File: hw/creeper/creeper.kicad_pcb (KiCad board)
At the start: 2 copper layers, 35 x 35 mm, 19 parts, among them SW1 EG1218, U1 ATtiny85V-10SU, U2 LIS2DH12TR

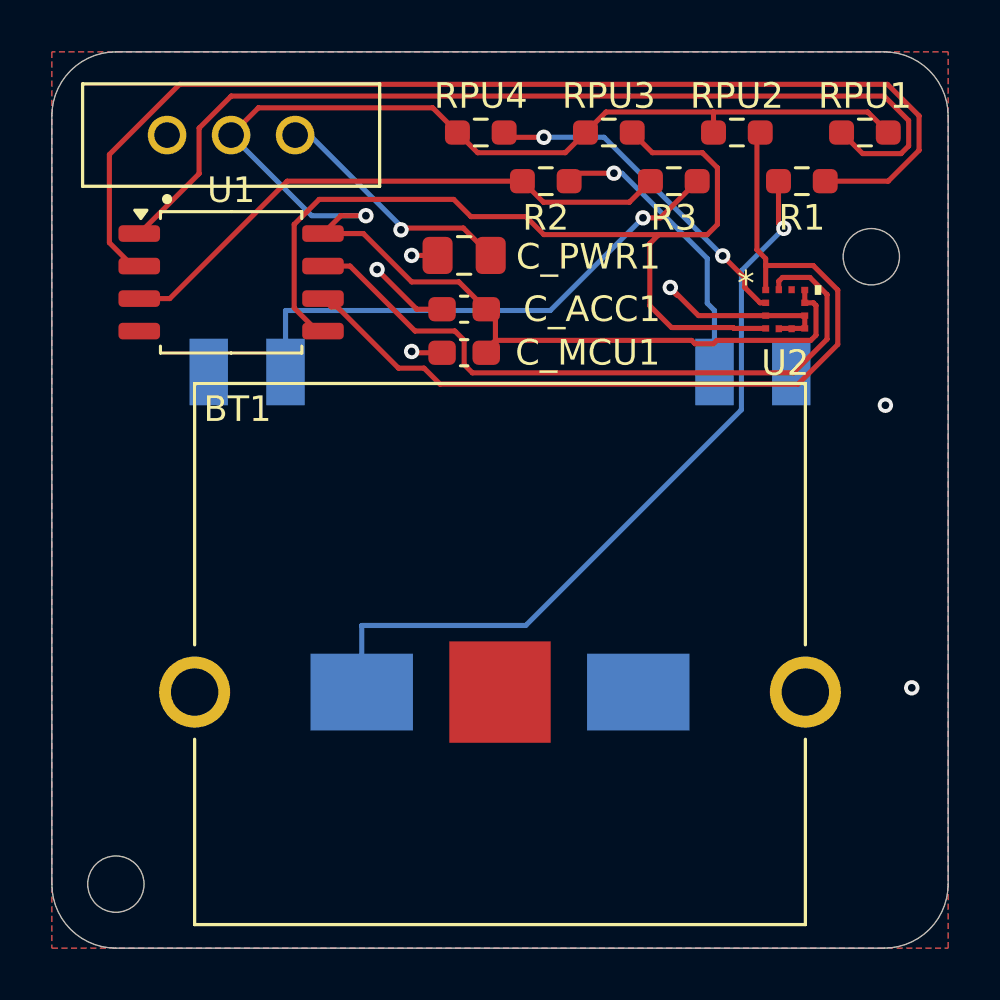
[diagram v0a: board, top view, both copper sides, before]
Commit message: feat(pcb): v0.7
* added TC2030_AVR pogo debug plug connector
* added isolating resistors to stabilize ISP
* fixed missing connections of battery holder
* added 0R bridge for always-on w/o switch
* moved mounting hole out of case opening
* did manual place and route
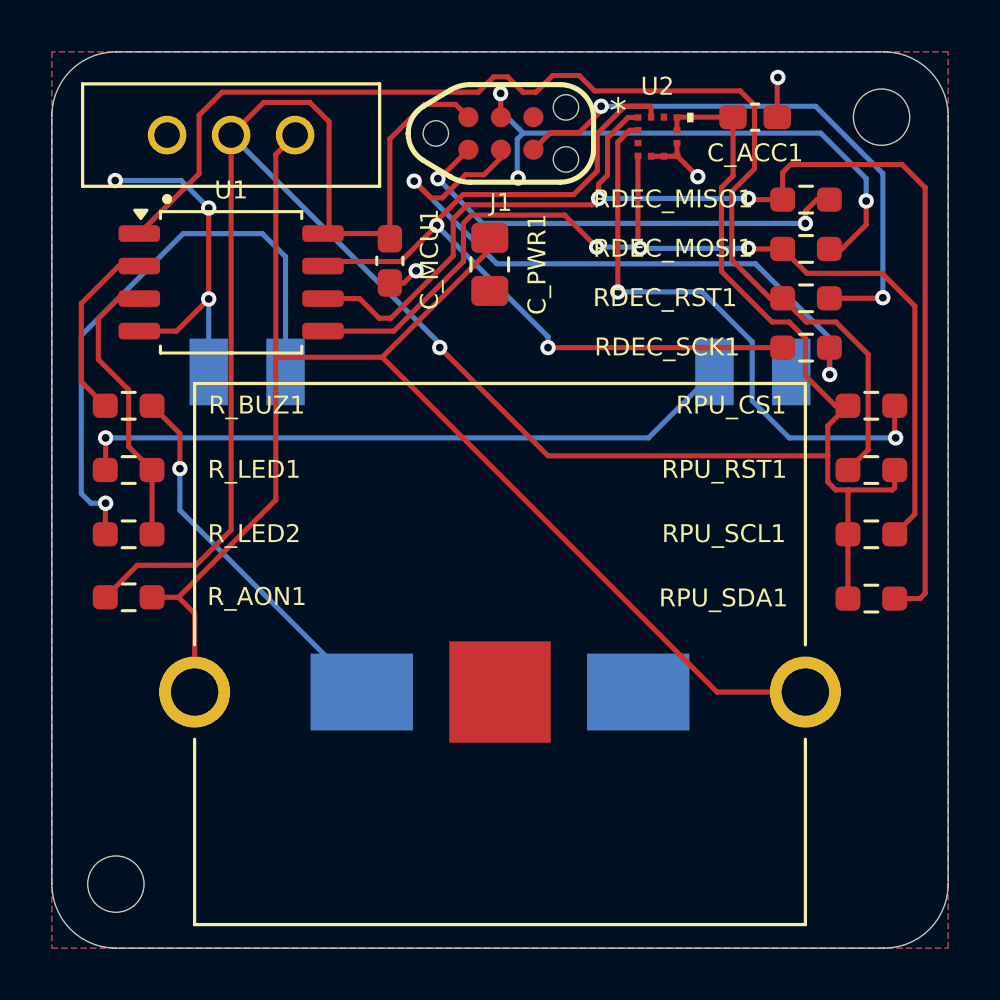
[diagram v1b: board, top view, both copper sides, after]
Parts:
- removed R1: 0R, Resistor_SMD:R_0603_1608Metric_Pad0.98x0.95mm_HandSolder
- removed R2, R3: 43R, Resistor_SMD:R_0603_1608Metric_Pad0.98x0.95mm_HandSolder
- removed RPU1, RPU2, RPU3, RPU4: 10K, Resistor_SMD:R_0603_1608Metric_Pad0.98x0.95mm_HandSolder
- added J1: TC2030_AVR, PCM_marbastlib-various:CON_TC2030_outlined, F.Cu at (117.5, 53.2)
- added RDEC_MISO1: 100R, Resistor_SMD:R_0603_1608Metric_Pad0.98x0.95mm_HandSolder, F.Cu at (129.4, 55.8)
- added RDEC_MOSI1: 100R, Resistor_SMD:R_0603_1608Metric_Pad0.98x0.95mm_HandSolder, F.Cu at (129.4, 57.7)
- added RDEC_RST1: 100R, Resistor_SMD:R_0603_1608Metric_Pad0.98x0.95mm_HandSolder, F.Cu at (129.4, 59.6)
- added RDEC_SCK1: 100R, Resistor_SMD:R_0603_1608Metric_Pad0.98x0.95mm_HandSolder, F.Cu at (129.4, 61.5)
- added RPU_CS1: 10K, Resistor_SMD:R_0603_1608Metric_Pad0.98x0.95mm_HandSolder, F.Cu at (132.0, 63.8)
- added RPU_RST1: 10K, Resistor_SMD:R_0603_1608Metric_Pad0.98x0.95mm_HandSolder, F.Cu at (132.0, 66.3)
- added RPU_SCL1: 10K, Resistor_SMD:R_0603_1608Metric_Pad0.98x0.95mm_HandSolder, F.Cu at (132.0, 68.8)
- added RPU_SDA1: 10K, Resistor_SMD:R_0603_1608Metric_Pad0.98x0.95mm_HandSolder, F.Cu at (132.0, 71.3)
- added R_AON1: 0R, Resistor_SMD:R_0603_1608Metric_Pad0.98x0.95mm_HandSolder, F.Cu at (103.0, 71.3)
- added R_BUZ1: 0R, Resistor_SMD:R_0603_1608Metric_Pad0.98x0.95mm_HandSolder, F.Cu at (103.0, 63.8)
- added R_LED1: 43R, Resistor_SMD:R_0603_1608Metric_Pad0.98x0.95mm_HandSolder, F.Cu at (103.0, 66.3)
- added R_LED2: 43R, Resistor_SMD:R_0603_1608Metric_Pad0.98x0.95mm_HandSolder, F.Cu at (103.0, 68.8)
- moved C_ACC1 13.6 mm to (127.5, 52.5), turned to 0 degrees
- moved U2 8.38 mm to (123.7, 53.3)
- moved REF**2 5.46 mm to (132.4, 52.5)
- moved C_MCU1 4.61 mm to (113.2, 58.2), turned to -90 degrees
- moved C_PWR1 1.06 mm to (117.1, 58.3), turned to -90 degrees
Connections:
- U1 pad 1: Net-(U1-~{RESET}/PB5) -> /~RESET
- U2 pad 3: GND -> unconnected-(U2-SDO/SA0-Pad3)
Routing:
- net Net-(BT1-+): track 9.72 -> 57.4 mm, vias 1 -> 0
- net /~RESET: track 0.00 -> 47.0 mm
- net Net-(U1-~{RESET}/PB5): track 37.8 -> 0.00 mm
- net /BUZZER: track 43.8 -> 7.25 mm
- net /+3V: track 61.6 -> 97.4 mm
- net Net-(J1-SCK): track 0.00 -> 25.9 mm, vias 0 -> 2
- net Net-(J1-MOSI): track 0.00 -> 22.5 mm, vias 0 -> 3
- net Net-(J1-~{RST}): track 0.00 -> 22.5 mm, vias 0 -> 2
- net Net-(J1-MISO): track 0.00 -> 18.3 mm, vias 0 -> 2
- net Net-(BZ1-+): track 30.6 -> 14.6 mm
- net /SCL: track 33.8 -> 49.3 mm, vias 0 -> 2
- net Net-(D1-A): track 11.5 -> 26.1 mm
- net /LED: track 22.5 -> 11.2 mm
- net Net-(U2-CS): track 13.2 -> 22.7 mm
- net GND: track 12.8 -> 19.2 mm
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
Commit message: feat: rev. 0.10: use analog switch for programmer isolation
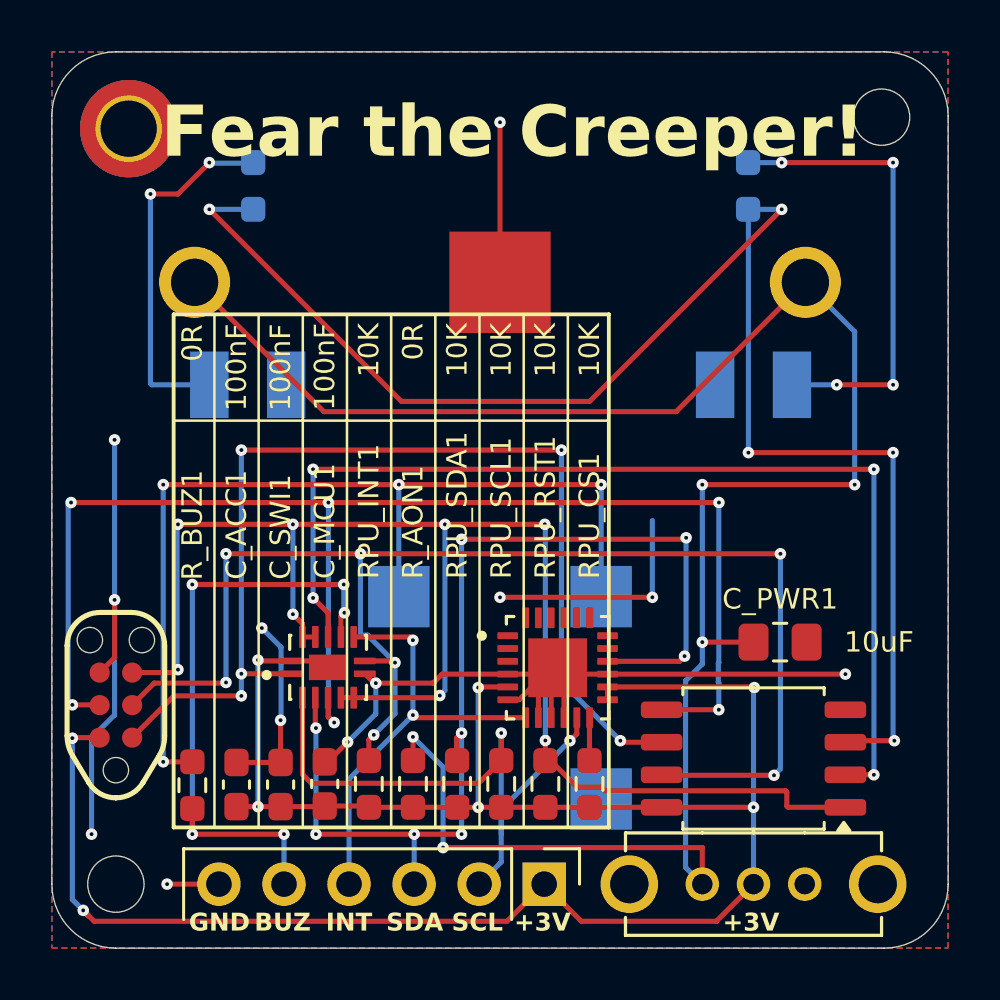
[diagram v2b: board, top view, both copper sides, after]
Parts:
- removed RDEC_MISO1, RDEC_MOSI1, RDEC_RST1, RDEC_SCK1: 100R, Resistor_SMD:R_0603_1608Metric_Pad0.98x0.95mm_HandSolder
- added C_SWI1: 100nF, creeper:C_0603_1608Metric_Pad1.08x0.95mm_HandSolder, F.Cu at (108.9, 78.6)
- added J2: Conn_01x06_Pin, creeper:PinHeader_1x06_P2.54mm_Vertical, F.Cu at (119.2, 82.5)
- added REF**: MountingHole_2.2mm_M2_DIN965_Pad_TopBottom, MountingHole:MountingHole_2.2mm_M2_DIN965_Pad_TopBottom, F.Cu at (103.0, 53.0)
- added RPU_INT1: 10K, creeper:R_0603_1608Metric_Pad0.98x0.95mm_HandSolder, F.Cu at (112.4, 78.6)
- added U3: ~, creeper:QFN50P300X250X100-15N, F.Cu at (110.8, 74.0)
- BZ1: value SMT-1324-TW-1V-HT-R -> ~; footprint creeper:XDCR_SMT-1324-TW-1V-HT-R -> creeper:XDCR_SMT-0825-S-2-R
- C_ACC1, C_MCU1: footprint Capacitor_SMD:C_0603_1608Metric_Pad1.08x0.95mm_HandSolder -> creeper:C_0603_1608Metric_Pad1.08x0.95mm_HandSolder
- C_PWR1: footprint Capacitor_SMD:C_0805_2012Metric_Pad1.18x1.45mm_HandSolder -> creeper:C_0805_2012Metric_Pad1.18x1.45mm_HandSolder
- RPU_CS1, RPU_RST1, RPU_SCL1, RPU_SDA1, R_AON1, R_BUZ1: footprint Resistor_SMD:R_0603_1608Metric_Pad0.98x0.95mm_HandSolder -> creeper:R_0603_1608Metric_Pad0.98x0.95mm_HandSolder
- R_LED1, R_LED2: value 43R -> 100R; footprint Resistor_SMD:R_0603_1608Metric_Pad0.98x0.95mm_HandSolder -> creeper:R_0603_1608Metric_Pad0.98x0.95mm_HandSolder; moved to B.Cu
- SW1: value EG1218 -> EG1213; footprint creeper:SW_EG1218 -> creeper:SW_EG1213
- U1: footprint Package_SO:SOIC-8_5.3x5.3mm_P1.27mm -> creeper:SOIC-8_5.3x5.3mm_P1.27mm
- U2: value LIS2DH12TR -> IIS328DQTR; footprint creeper:LGA-12_STM -> creeper:IIS328DQTR_QFN50P400X400X185-25N
- moved SW1 35.7 mm to (127.4, 82.5), turned to 180 degrees
- moved C_ACC1 33.0 mm to (107.2, 78.6), turned to 90 degrees
- moved U1 27.6 mm to (127.4, 77.6), turned to 180 degrees
- moved J1 26.9 mm to (102.5, 75.5), turned to 90 degrees
- moved R_LED1 26.6 mm to (127.2, 55.2), turned to -90 degrees
- moved U2 21.1 mm to (119.8, 74.0)
- moved C_MCU1 20.6 mm to (110.7, 78.6), turned to 90 degrees
- moved C_PWR1 18.6 mm to (128.4, 73.0), turned to 0 degrees
- moved RPU_CS1 18.4 mm to (121.0, 78.6), turned to -90 degrees
- moved RPU_SDA1 17.7 mm to (115.8, 78.6), turned to 90 degrees
- moved RPU_RST1 17.7 mm to (119.3, 78.6), turned to 90 degrees
- moved RPU_SCL1 17.4 mm to (117.5, 78.6), turned to 90 degrees
- moved BT1 16.0 mm to (117.5, 59.0), turned to 180 degrees
- moved R_BUZ1 15.0 mm to (105.5, 78.6), turned to 90 degrees
- moved R_LED2 14.4 mm to (107.9, 55.2), turned to -90 degrees
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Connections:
- net /LED renamed /LED_MCU
- J1 pad 1: Net-(J1-MISO) -> /SCL_MCU
- J1 pad 3: Net-(J1-SCK) -> /INT_MCU
- J1 pad 4: Net-(J1-MOSI) -> /SDA_MCU
- J1 pad 5: Net-(J1-~{RST}) -> /~RESET
- RPU_CS1 pad 1: /+3V -> Net-(U2-CS)
- RPU_CS1 pad 2: Net-(U2-CS) -> /+3V
- RPU_RST1 pad 1: /~RESET -> /+3V
- RPU_RST1 pad 2: /+3V -> /~RESET
- RPU_SCL1 pad 2: /SDA -> /SCL1
- RPU_SDA1 pad 2: /SCL -> /SDA1
- R_BUZ1 pad 1: /BUZZER -> /BUZ
- U1 pad 2: /BUZZER -> /BUZ_MCU
- U1 pad 5: /SDA -> /SDA_MCU
- U1 pad 6: /SCL -> /SCL_MCU
- U1 pad 7: /INT -> /INT_MCU
- U2 pad 1: /SCL -> (no net)
- U2 pad 10: /+3V -> GND
- U2 pad 11: unconnected-(U2-INT2-Pad11) -> /SCL1
- U2 pad 12: /INT -> Net-(U2-CS)
- U2 pad 2: Net-(U2-CS) -> (no net)
- U2 pad 4: /SDA -> GND
- U2 pad 5: GND -> /+3V
- U2 pad 7: GND -> /INT
- U2 pad 9: /+3V -> GND
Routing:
- net GND: track 19.2 -> 74.7 mm, vias 6 -> 12
- net /INT_MCU: track 0.00 -> 54.2 mm, vias 0 -> 7
- net /SDA_MCU: track 0.00 -> 54.2 mm, vias 0 -> 6
- net /SCL: track 49.3 -> 0.00 mm, vias 2 -> 0
- net /LED_MCU: track 11.2 -> 59.6 mm, vias 0 -> 5
- net /SCL_MCU: track 0.00 -> 42.8 mm, vias 0 -> 5
- net /SDA1: track 0.00 -> 42.0 mm, vias 0 -> 8
- net /BUZ_MCU: track 0.00 -> 41.7 mm, vias 0 -> 4
- net /SDA: track 40.2 -> 0.00 mm, vias 3 -> 0
- net Net-(J1-SCK): track 25.9 -> 0.00 mm, vias 2 -> 0
- net /SCL1: track 0.00 -> 24.4 mm, vias 0 -> 2
- net /BUZ: track 0.00 -> 24.2 mm, vias 0 -> 5
- net Net-(BZ1-Pad1): track 14.6 -> 37.7 mm, vias 1 -> 4
- net Net-(J1-MOSI): track 22.5 -> 0.00 mm, vias 3 -> 0
- net Net-(J1-~{RST}): track 22.5 -> 0.00 mm, vias 2 -> 0
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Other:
- board text added: "+3V"
- board text added: "BUZ"
- board text added: "GND"
- board text added: "INT"
- board text added: "SCL"
- board text added: "SDA"

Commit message: feat(pcb): update constraints, fix via sizes
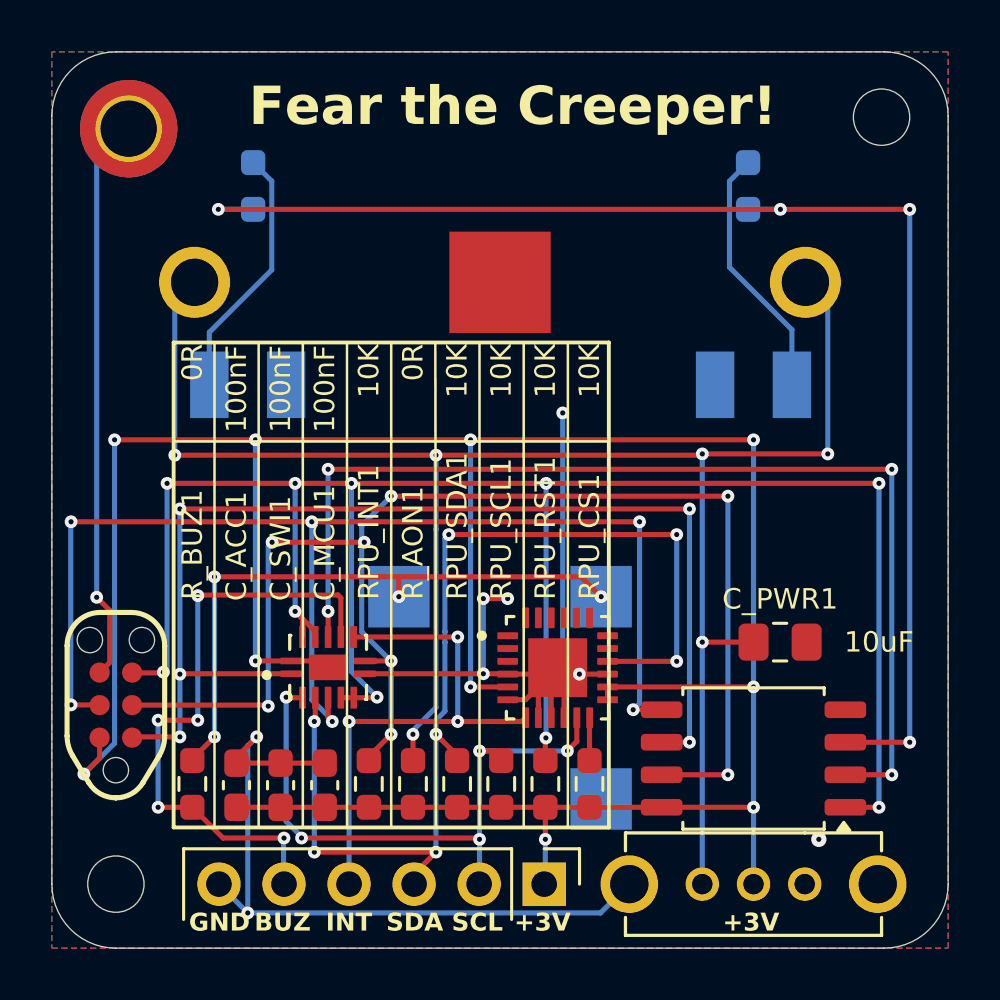
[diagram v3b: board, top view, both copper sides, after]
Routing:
- net /+3V: track 85.3 -> 109.6 mm, vias 8 -> 10
- net /~RESET: track 59.4 -> 79.0 mm, vias 8 -> 10
- net Net-(BZ1-Pad1): track 37.7 -> 23.8 mm
- net GND: track 74.7 -> 83.1 mm, vias 12 -> 9
- net Net-(D1-A): track 18.2 -> 9.99 mm, vias 4 -> 0
- net Net-(BT1-+): track 78.2 -> 70.8 mm, vias 5 -> 6
- net /LED_MCU: track 59.6 -> 53.0 mm, vias 5 -> 4
- net /SDA_MCU: track 54.2 -> 48.2 mm
- net Net-(D2-A): track 14.2 -> 9.99 mm, vias 2 -> 0
- net /INT: track 17.4 -> 20.6 mm, vias 2 -> 3
- net /SCL_MCU: track 42.8 -> 45.2 mm
- net /SDA1: track 42.0 -> 42.9 mm, vias 8 -> 7
- net /INT_MCU: track 54.2 -> 55.0 mm, vias 7 -> 8
- net /BUZ_MCU: track 41.7 -> 42.3 mm
- net /SCL1: track 24.4 -> 24.5 mm, vias 2 -> 5
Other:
- rule pad_to_mask_clearance: 0 -> 0.05

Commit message: feat: v0.11: replace accelerometer with optional spring vibration sensor
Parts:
- added QR*****: https://github.com/jkorinth/fear_the_creeper, creeper:github_jkorinth-fear_the_creeper, B.Cu at (129.5, 76.1)
- added RPU_SVS1: 10K, creeper:R_0603_1608Metric_Pad0.98x0.95mm_HandSolder, B.Cu at (111.0, 54.6)
- added SVS1: SW_Push, creeper:SW_180xxP_Spring_Vibration_Sensor, B.Cu at (103.4, 68.2)
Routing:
- net Net-(RPU_SVS1-Pad1): track 0.00 -> 17.8 mm, vias 0 -> 2
- net /INT: track 20.6 -> 34.5 mm, vias 3 -> 6
- net GND: track 83.1 -> 93.8 mm, vias 9 -> 11
- net /~RESET: track 79.0 -> 68.8 mm, vias 10 -> 9
- net /+3V: track 109.6 -> 101.9 mm
- net Net-(BT1-+): track 70.8 -> 69.8 mm

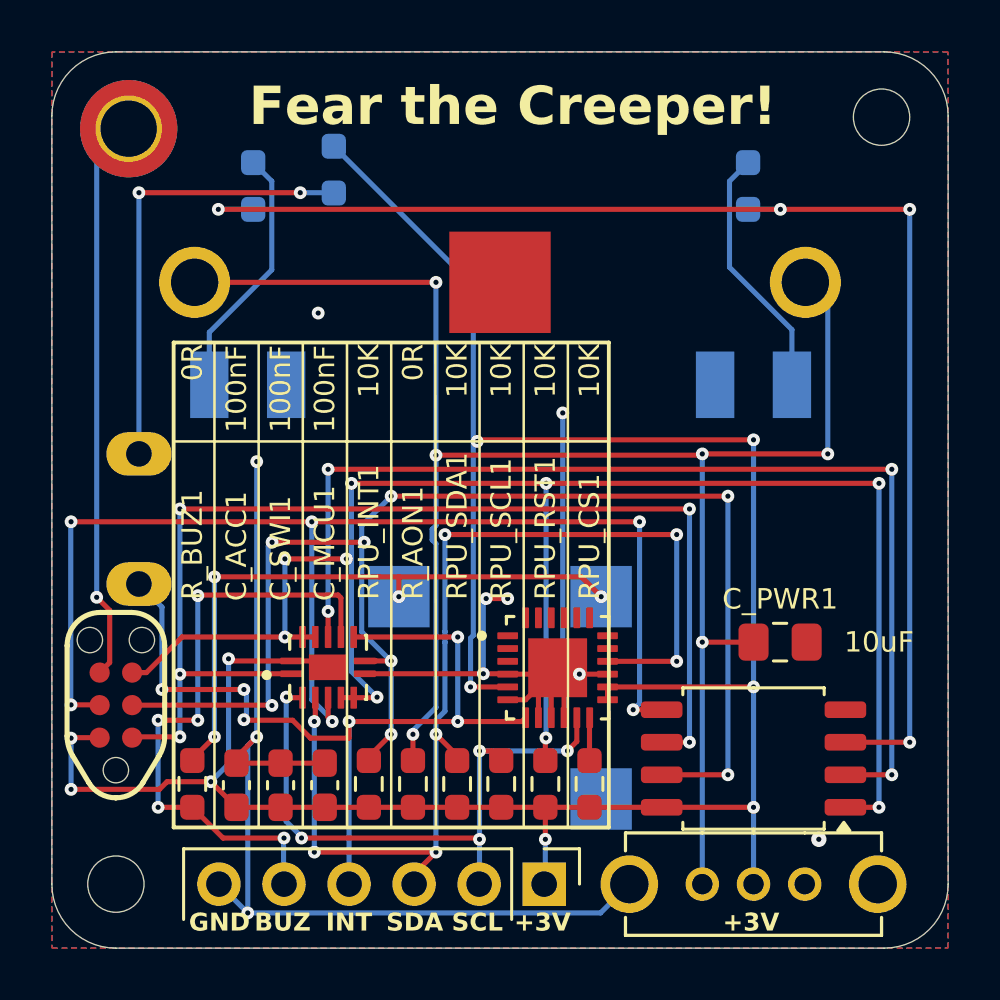
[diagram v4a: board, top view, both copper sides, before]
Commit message: fix(sch+pcb): update footprints, reset DNP
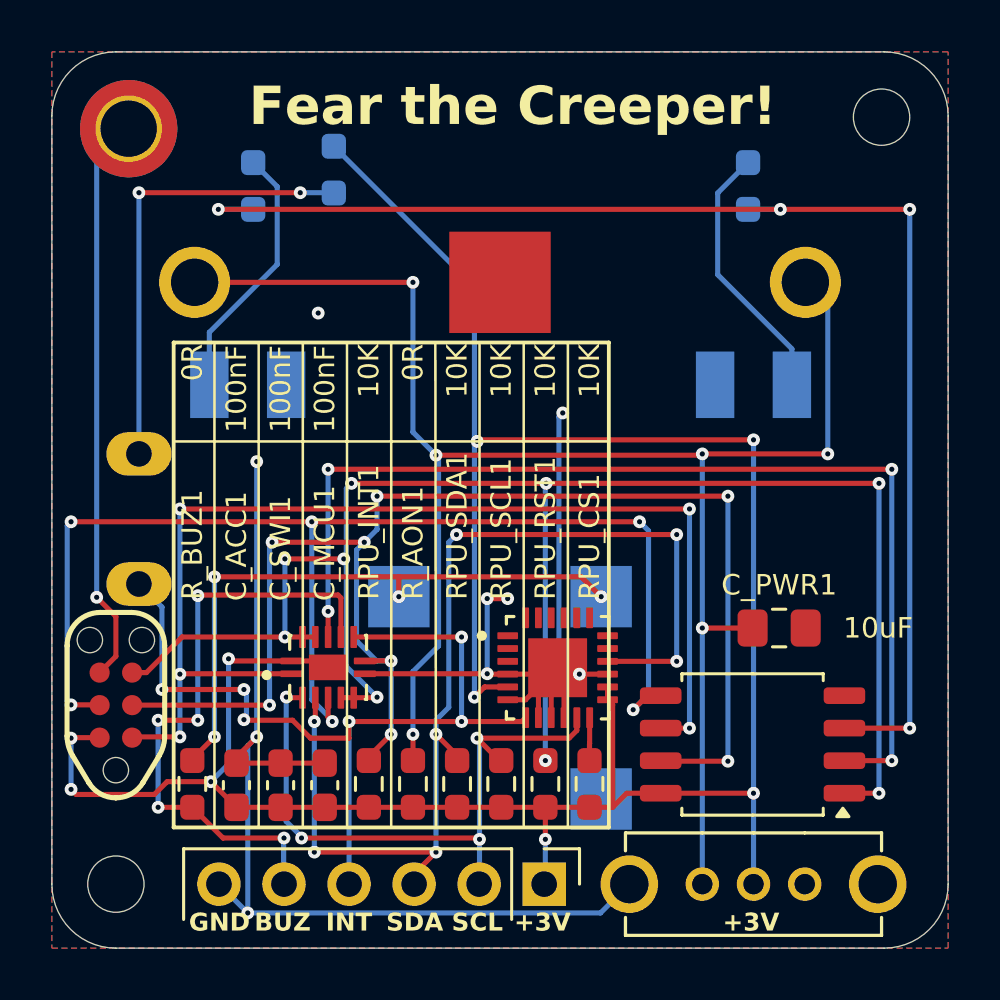
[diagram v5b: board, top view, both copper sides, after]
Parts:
- moved U1 0.55 mm to (127.4, 77.0)
- moved C_PWR1 0.55 mm to (128.4, 72.5)
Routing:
- net /+3V: track 101.9 -> 101.2 mm, vias 10 -> 9
- net Net-(BT1-+): track 69.8 -> 69.2 mm
- net /SDA_MCU: track 48.2 -> 48.8 mm
- net /LED_MCU: track 53.0 -> 52.4 mm
- net /SCL_MCU: track 45.2 -> 44.7 mm
- net /BUZ_MCU: track 42.3 -> 41.8 mm
- net /SCL1: track 24.5 -> 24.9 mm, vias 5 -> 4
- net GND: track 93.8 -> 94.1 mm, vias 11 -> 10
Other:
- rule pad_to_mask_clearance: 0.05 -> 0
